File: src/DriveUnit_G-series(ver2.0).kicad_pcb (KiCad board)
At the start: 2 copper layers, 65.7 x 21.5 mm, 1 part

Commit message: [add]配線途中まで
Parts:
- added C1: 100n, Capacitor_SMD:C_0603_1608Metric_Pad1.08x0.95mm_HandSolder, F.Cu at (170.5, 111.0)
- added C10: 220u, Symbol:U2-R_NCH, B.Cu at (191.4, 112.5)
- added C2: 100n, Capacitor_SMD:C_0603_1608Metric_Pad1.08x0.95mm_HandSolder, F.Cu at (170.5, 116.0)
- added C3: 100n, Capacitor_SMD:C_0603_1608Metric_Pad1.08x0.95mm_HandSolder, F.Cu at (166.9, 113.5)
- added C4: 100n, Capacitor_SMD:C_0603_1608Metric_Pad1.08x0.95mm_HandSolder, F.Cu at (147.4, 114.0)
- added C5: 100n, Capacitor_SMD:C_0603_1608Metric_Pad1.08x0.95mm_HandSolder, F.Cu at (147.4, 120.4)
- added C6: 470n, Capacitor_SMD:C_0805_2012Metric_Pad1.18x1.45mm_HandSolder, F.Cu at (161.4, 120.0)
- added C7: 100n, Capacitor_SMD:C_0603_1608Metric_Pad1.08x0.95mm_HandSolder, F.Cu at (147.4, 118.8)
- added C8: 100n, Capacitor_SMD:C_0603_1608Metric_Pad1.08x0.95mm_HandSolder, F.Cu at (147.4, 115.6)
- added C9: 2.2u, Capacitor_SMD:C_0603_1608Metric_Pad1.08x0.95mm_HandSolder, F.Cu at (147.4, 117.2)
- added D1: LED, LED_SMD:LED_0603_1608Metric_Pad1.05x0.95mm_HandSolder, F.Cu at (121.3, 108.4)
- added D2: LED, LED_SMD:LED_0603_1608Metric_Pad1.05x0.95mm_HandSolder, F.Cu at (125.3, 108.4)
- added D3: LED, LED_SMD:LED_0603_1608Metric_Pad1.05x0.95mm_HandSolder, F.Cu at (168.8, 120.0)
- added D4: LED, LED_SMD:LED_0603_1608Metric_Pad1.05x0.95mm_HandSolder, F.Cu at (150.6, 108.2)
- added D5: LED, LED_SMD:LED_0603_1608Metric_Pad1.05x0.95mm_HandSolder, F.Cu at (157.2, 108.2)
- added IC1: A3921, Symbol:A3921, F.Cu at (152.0, 112.4)
- added Q1: SQJA16EP-T1_GE3, Symbol:SQJA16EP-T1_GE3, F.Cu at (134.8, 112.5)
- added Q2: SQJA16EP-T1_GE3, Symbol:SQJA16EP-T1_GE3, F.Cu at (122.8, 119.0)
- added Q3: SQJA16EP-T1_GE3, Symbol:SQJA16EP-T1_GE3, F.Cu at (122.8, 112.2)
- added Q4: SQJA16EP-T1_GE3, Symbol:SQJA16EP-T1_GE3, F.Cu at (134.8, 119.0)
- added Q5: Q_NPN_BCE, Package_TO_SOT_SMD:SOT-23-3, F.Cu at (146.2, 109.2)
- added Q6: Q_NPN_BCE, Package_TO_SOT_SMD:SOT-23-3, F.Cu at (161.4, 110.8)
- added R1: 200, Resistor_SMD:R_0603_1608Metric_Pad0.98x0.95mm_HandSolder, F.Cu at (179.0, 120.5)
- added R10: 10, Resistor_SMD:R_0603_1608Metric_Pad0.98x0.95mm_HandSolder, F.Cu at (143.9, 112.4)
- added R11: 1k, Resistor_SMD:R_0603_1608Metric_Pad0.98x0.95mm_HandSolder, F.Cu at (130.7, 108.4)
- added R12: 10, Resistor_SMD:R_0603_1608Metric_Pad0.98x0.95mm_HandSolder, F.Cu at (143.9, 117.2)
- added R13: 100k, Resistor_SMD:R_0603_1608Metric_Pad0.98x0.95mm_HandSolder, F.Cu at (147.4, 112.4)
- added R14: 100k, Resistor_SMD:R_0603_1608Metric_Pad0.98x0.95mm_HandSolder, F.Cu at (161.4, 108.2)
- added R15: 10k, Resistor_SMD:R_0603_1608Metric_Pad0.98x0.95mm_HandSolder, F.Cu at (138.2, 111.7)
- added R16: 10k, Resistor_SMD:R_0603_1608Metric_Pad0.98x0.95mm_HandSolder, F.Cu at (126.5, 118.5)
- added R17: 10k, Resistor_SMD:R_0603_1608Metric_Pad0.98x0.95mm_HandSolder, F.Cu at (138.2, 118.5)
- added R18: 10k, Resistor_SMD:R_0603_1608Metric_Pad0.98x0.95mm_HandSolder, F.Cu at (126.5, 111.7)
- added R19: 10, Resistor_SMD:R_0603_1608Metric_Pad0.98x0.95mm_HandSolder, F.Cu at (143.9, 114.0)
- added R2: 200, Resistor_SMD:R_0603_1608Metric_Pad0.98x0.95mm_HandSolder, F.Cu at (177.0, 120.5)
- added R20: 10, Resistor_SMD:R_0603_1608Metric_Pad0.98x0.95mm_HandSolder, F.Cu at (143.9, 115.6)
- added R21: 10k, Resistor_SMD:R_0603_1608Metric_Pad0.98x0.95mm_HandSolder, F.Cu at (147.4, 122.0)
- added R3: 1k, Resistor_SMD:R_0603_1608Metric_Pad0.98x0.95mm_HandSolder, F.Cu at (173.0, 120.0)
- added R4: 200, Resistor_SMD:R_0603_1608Metric_Pad0.98x0.95mm_HandSolder, F.Cu at (153.1, 109.1)
- added R5: 200, Resistor_SMD:R_0603_1608Metric_Pad0.98x0.95mm_HandSolder, F.Cu at (154.6, 109.1)
- added R6: 3k, Resistor_SMD:R_0603_1608Metric_Pad0.98x0.95mm_HandSolder, F.Cu at (161.0, 113.4)
- added R7: 10k, Resistor_SMD:R_0603_1608Metric_Pad0.98x0.95mm_HandSolder, F.Cu at (150.6, 110.4)
- added R8: 10k, Resistor_SMD:R_0603_1608Metric_Pad0.98x0.95mm_HandSolder, F.Cu at (157.2, 110.4)
- added R9: 10k, Resistor_SMD:R_0603_1608Metric_Pad0.98x0.95mm_HandSolder, F.Cu at (161.0, 115.3)
- added SB1: V2P22LHM3/H, Symbol:V2P22LHM3_H, F.Cu at (128.6, 119.2)
- added SB2: V2P22LHM3/H, Symbol:V2P22LHM3_H, F.Cu at (140.5, 119.2)
- added SB3: V2P22LHM3/H, Symbol:V2P22LHM3_H, F.Cu at (140.5, 112.4)
- added SB4: V2P22LHM3/H, Symbol:V2P22LHM3_H, F.Cu at (128.8, 112.5)
- added SW3: THAF01-NC-R, Symbol:THAF01-NC-R, F.Cu at (168.6, 108.0)
- added TLP1: TLP2366, Symbol:TLP2366, F.Cu at (179.2, 112.3)
- added TLP2: TLP2366, Symbol:TLP2366, F.Cu at (179.2, 117.3)
- added U2: TC7S14F, Symbol:TC7S14F, F.Cu at (167.0, 116.0)
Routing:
- net /V5: track 0.00 -> 25.8 mm
- net /DIR: track 0.00 -> 21.4 mm
- net /RESET: track 0.00 -> 14.9 mm
- net /PWM: track 0.00 -> 9.30 mm
- net Net-(TLP1-ANODE): track 0.00 -> 8.42 mm
- net /GLA: track 0.00 -> 7.91 mm
- net Net-(IC1-CP1): track 0.00 -> 6.19 mm
- net /PWM_IN: track 0.00 -> 5.56 mm
- net Net-(IC1-CB): track 0.00 -> 5.25 mm
- net Net-(IC1-CA): track 0.00 -> 5.06 mm
- net Net-(TLP2-VOUT): track 0.00 -> 4.65 mm
- net Net-(IC1-VREG): track 0.00 -> 4.54 mm
- net /FF2: track 0.00 -> 4.12 mm
- net Net-(IC1-CP2): track 0.00 -> 3.51 mm
- net Net-(TLP2-ANODE): track 0.00 -> 3.21 mm
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- added copper zone on B.Cu, net /SA
- added copper zone on F.Cu, net /SA
- added copper zone on B.Cu, net /SB
- added copper zone on F.Cu, net /SB
- added copper zone on B.Cu, net VCC
- added copper zone on F.Cu, net VCC
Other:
- board size 65.7 x 21.5 mm -> 65.7 x 23.3 mm

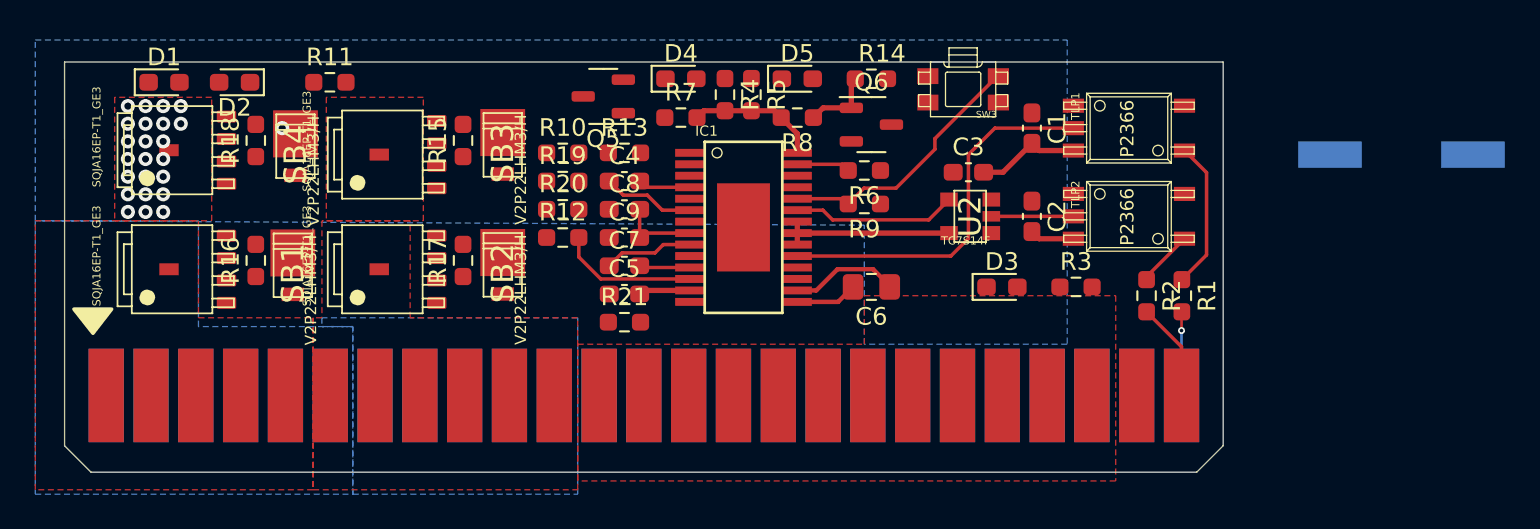
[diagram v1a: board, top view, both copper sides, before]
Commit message: [add]電源ライン以外の配線完了
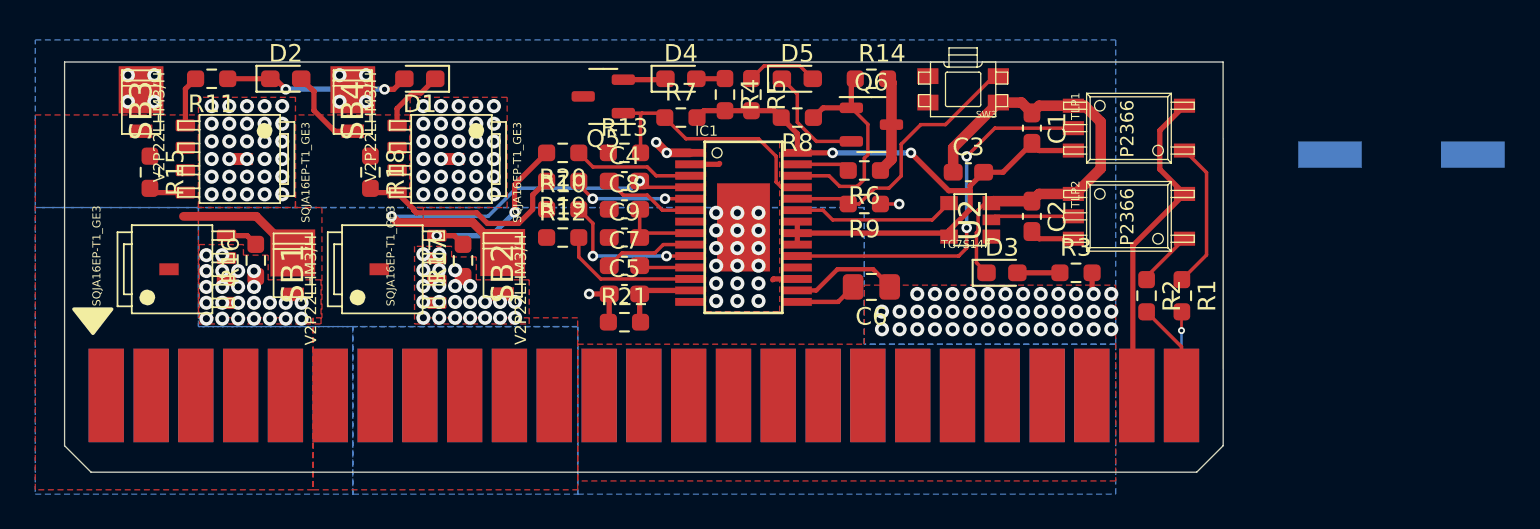
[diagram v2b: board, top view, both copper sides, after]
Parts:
- moved SB3 20.6 mm to (120.0, 110.0)
- moved R15 17.8 mm to (120.5, 113.5), turned to -90 degrees
- moved D1 14.5 mm to (135.8, 108.2), turned to 180 degrees
- moved Q3 13.7 mm to (136.5, 112.8), turned to -90 degrees
- moved Q1 10.3 mm to (124.5, 112.8), turned to -90 degrees
- moved R18 6.74 mm to (133.0, 113.5), turned to -90 degrees
- moved R11 6.70 mm to (124.0, 108.2), turned to 180 degrees
- moved SB4 4.10 mm to (132.0, 110.0)
- moved R10 3.20 mm to (143.9, 115.6)
- moved R20 3.20 mm to (143.9, 112.4), turned to 180 degrees
- moved D2 2.91 mm to (128.2, 108.2), turned to 0 degrees
- moved D3 0.80 mm to (168.8, 119.2)
- moved R3 0.80 mm to (173.0, 119.2)
- moved U2 0.20 mm to (167.0, 116.2)
- turned R19 to 180 degrees
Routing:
- net GND: track 0.00 -> 37.5 mm, vias 0 -> 66
- net /SB: track 2.98 -> 33.6 mm, vias 0 -> 2
- net /GND_IN: track 0.11 -> 19.0 mm
- net /V5: track 25.8 -> 41.1 mm, vias 0 -> 2
- net /FF1: track 0.00 -> 14.8 mm
- net Net-(Q3-PadG): track 0.00 -> 12.3 mm
- net Net-(Q4-PadG): track 0.00 -> 10.8 mm, vias 0 -> 2
- net Net-(D1-A): track 0.00 -> 10.5 mm, vias 0 -> 2
- net /SA: track 2.88 -> 12.8 mm
- net /FF2: track 4.12 -> 12.9 mm
- net /GHA: track 0.00 -> 8.47 mm, vias 0 -> 2
- net /GHB: track 0.00 -> 6.83 mm, vias 0 -> 2
- net /GLB: track 0.00 -> 6.83 mm
- net Net-(D5-K): track 0.00 -> 6.34 mm
- net VCC: track 2.92 -> 8.99 mm, vias 24 -> 111
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- added copper zone on B.Cu, net GND
- added copper zone on F.Cu, net GND

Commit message: [complete]配線完了
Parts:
- moved C10 16.1 mm to (175.4, 113.0), turned to 0 degrees
- moved C6 0.80 mm to (161.4, 120.8)
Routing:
- net GND: track 37.5 -> 94.8 mm, vias 66 -> 69
- net Net-(Q2-PadG): track 1.86 -> 33.4 mm, vias 0 -> 2
- net /SA: track 12.8 -> 37.9 mm, vias 0 -> 27
- net Net-(Q1-PadG): track 2.11 -> 24.2 mm, vias 0 -> 2
- net VCC: track 8.99 -> 16.1 mm, vias 111 -> 107
- net /V5: track 41.1 -> 47.5 mm
- net /GHB: track 6.83 -> 8.45 mm
- net /SB: vias 2 -> 26

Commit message: [wip]DRC全通過完了
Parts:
- moved C7 0.20 mm to (147.4, 119.0)
- moved R21 0.20 mm to (147.4, 122.2)
- moved C5 0.20 mm to (147.4, 120.6)
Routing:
- net /GLA: track 7.91 -> 8.46 mm

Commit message: :tada:完成
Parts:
- added G***: LOGO, LOGO, B.Cu at (139.6, 119.4)
- added G***: LOGO, LOGO, B.Cu at (156.4, 114.0)
- moved R18 10.7 mm to (142.8, 109.2)
- moved SB1 0.55 mm to (128.6, 119.8)
- moved Q1 0.40 mm to (124.1, 112.8)
- moved R7 0.40 mm to (150.6, 110.8)
- moved R8 0.40 mm to (157.2, 110.8)
- renumbered D4 to FF1, D5 to FF2, D2 to MA, D1 to MB, D3 to POWER, SW3 to RESET
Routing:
- net /SB: track 33.6 -> 39.8 mm
- net Net-(Q3-PadG): track 12.3 -> 15.7 mm
- net /SA: track 38.0 -> 38.8 mm
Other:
- board text added: "53"
- board text added: "HOW TO USE"
- board text added: "MOEL"
- board text added: "Note:"
- board text added: "ver 1.0"

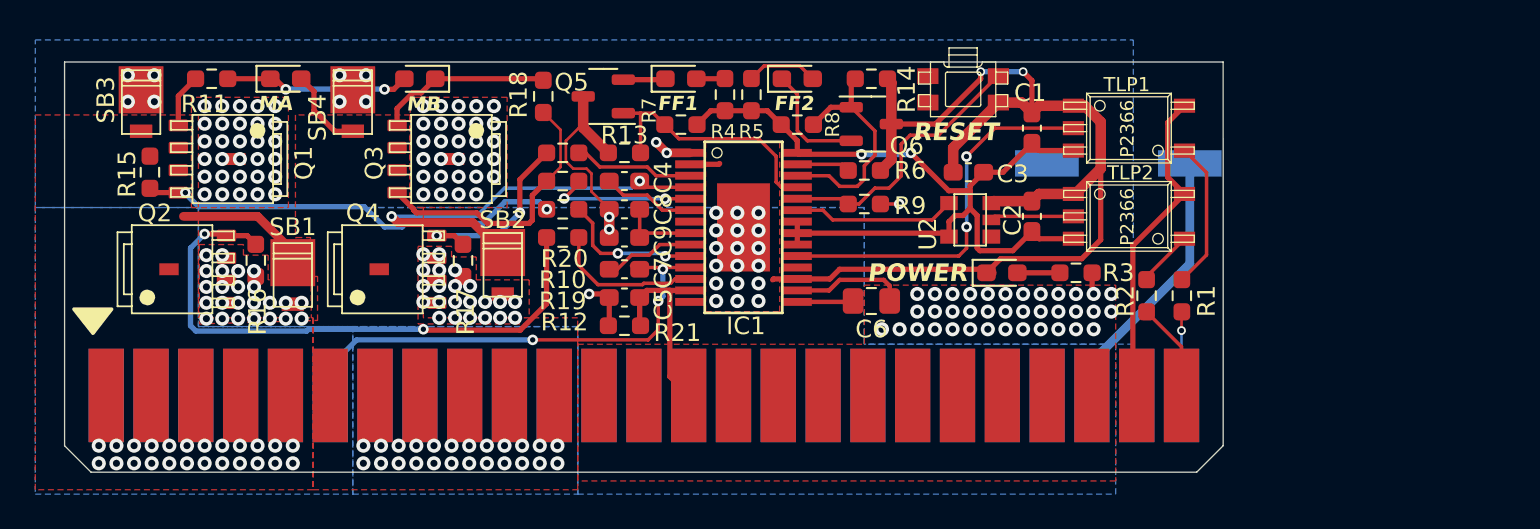
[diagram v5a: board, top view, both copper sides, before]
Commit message: [fix]部品配置微修正
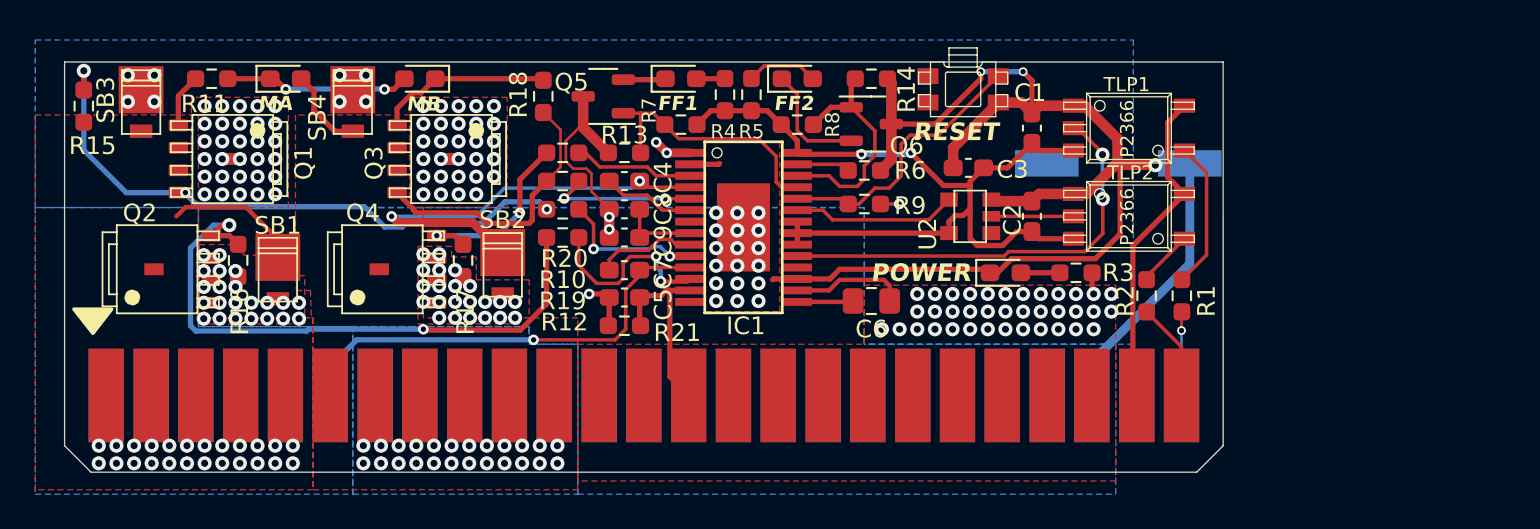
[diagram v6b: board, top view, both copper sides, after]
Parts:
- moved R15 5.30 mm to (116.8, 109.8), turned to 90 degrees
- moved R16 1.00 mm to (125.5, 118.5)
- moved SB1 0.90 mm to (127.8, 119.5)
- moved Q2 0.85 mm to (122.0, 119.0)
- moved C3 0.25 mm to (166.9, 113.2)
- moved U2 0.20 mm to (167.0, 116.0)
- moved POWER 0.20 mm to (169.0, 119.2)
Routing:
- net Net-(Q1-PadG): track 24.2 -> 34.9 mm, vias 2 -> 3
- net GND: track 94.9 -> 101.9 mm, vias 69 -> 68
- net /DIR: track 21.7 -> 24.7 mm
- net /GLA: track 8.46 -> 10.8 mm, vias 0 -> 2
- net Net-(Q2-PadG): track 33.4 -> 34.9 mm
- net /SA: track 38.8 -> 37.4 mm, vias 27 -> 25
- net Net-(IC1-CA): track 5.14 -> 5.75 mm
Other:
- board text removed: "ver 2.0"
